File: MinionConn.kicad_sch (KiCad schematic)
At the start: 16 parts, among them J1 MinionConn, U2 EL817

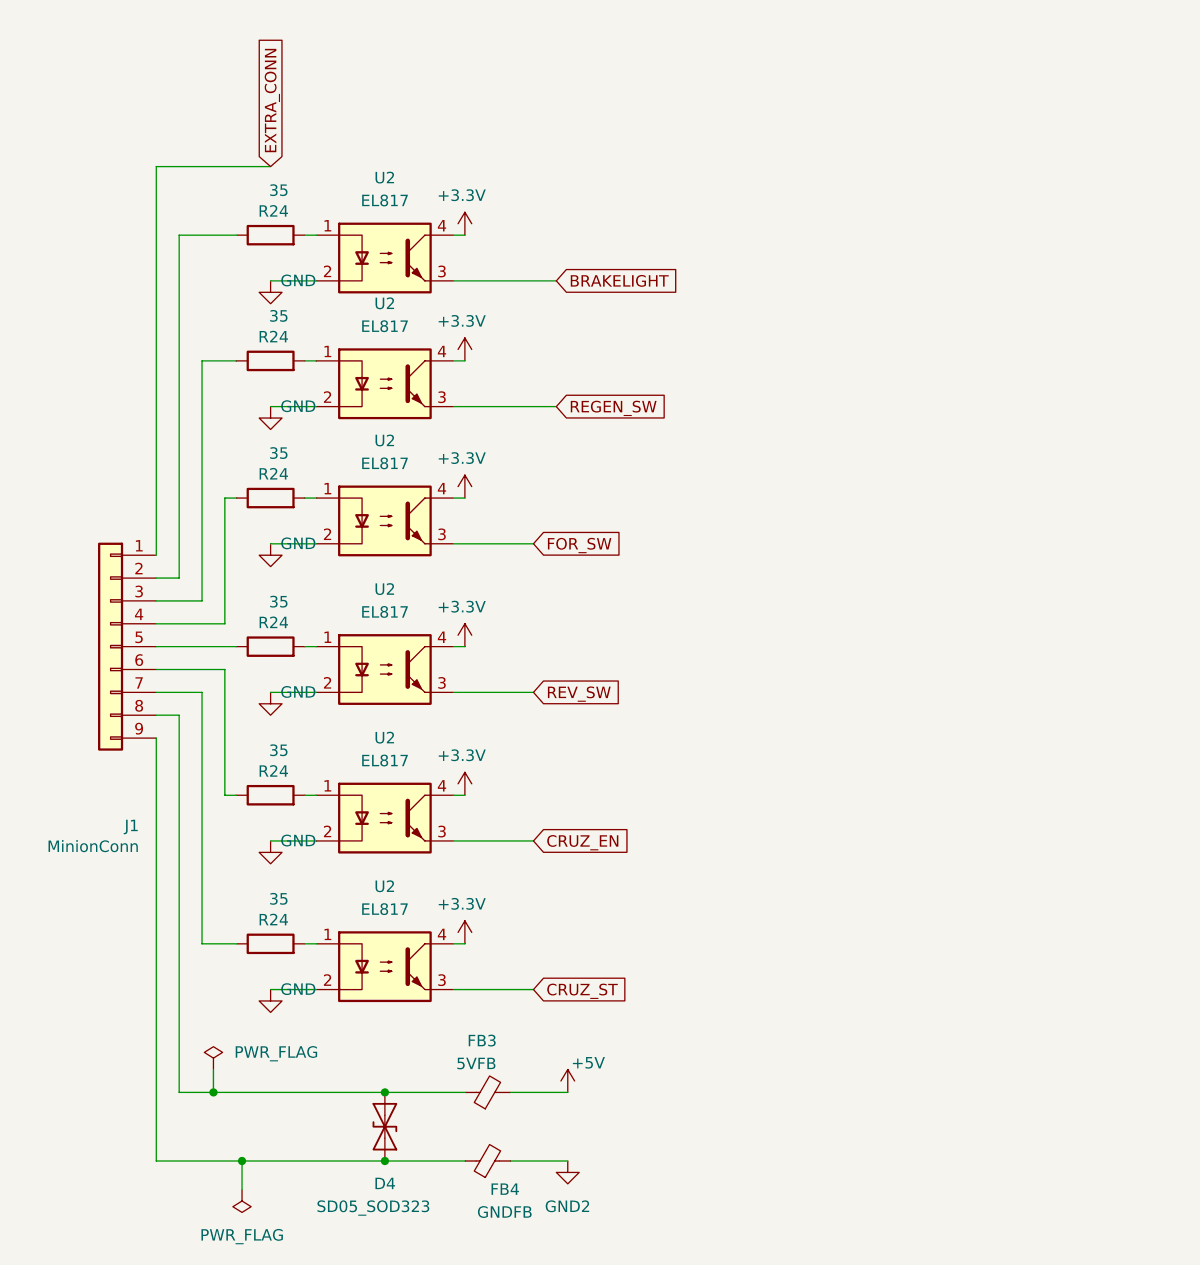
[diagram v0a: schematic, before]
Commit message: Opto-Isolators now interface mosfets to avoid ground problems, also separated 12V 'power' ground and ground passed from minion connector
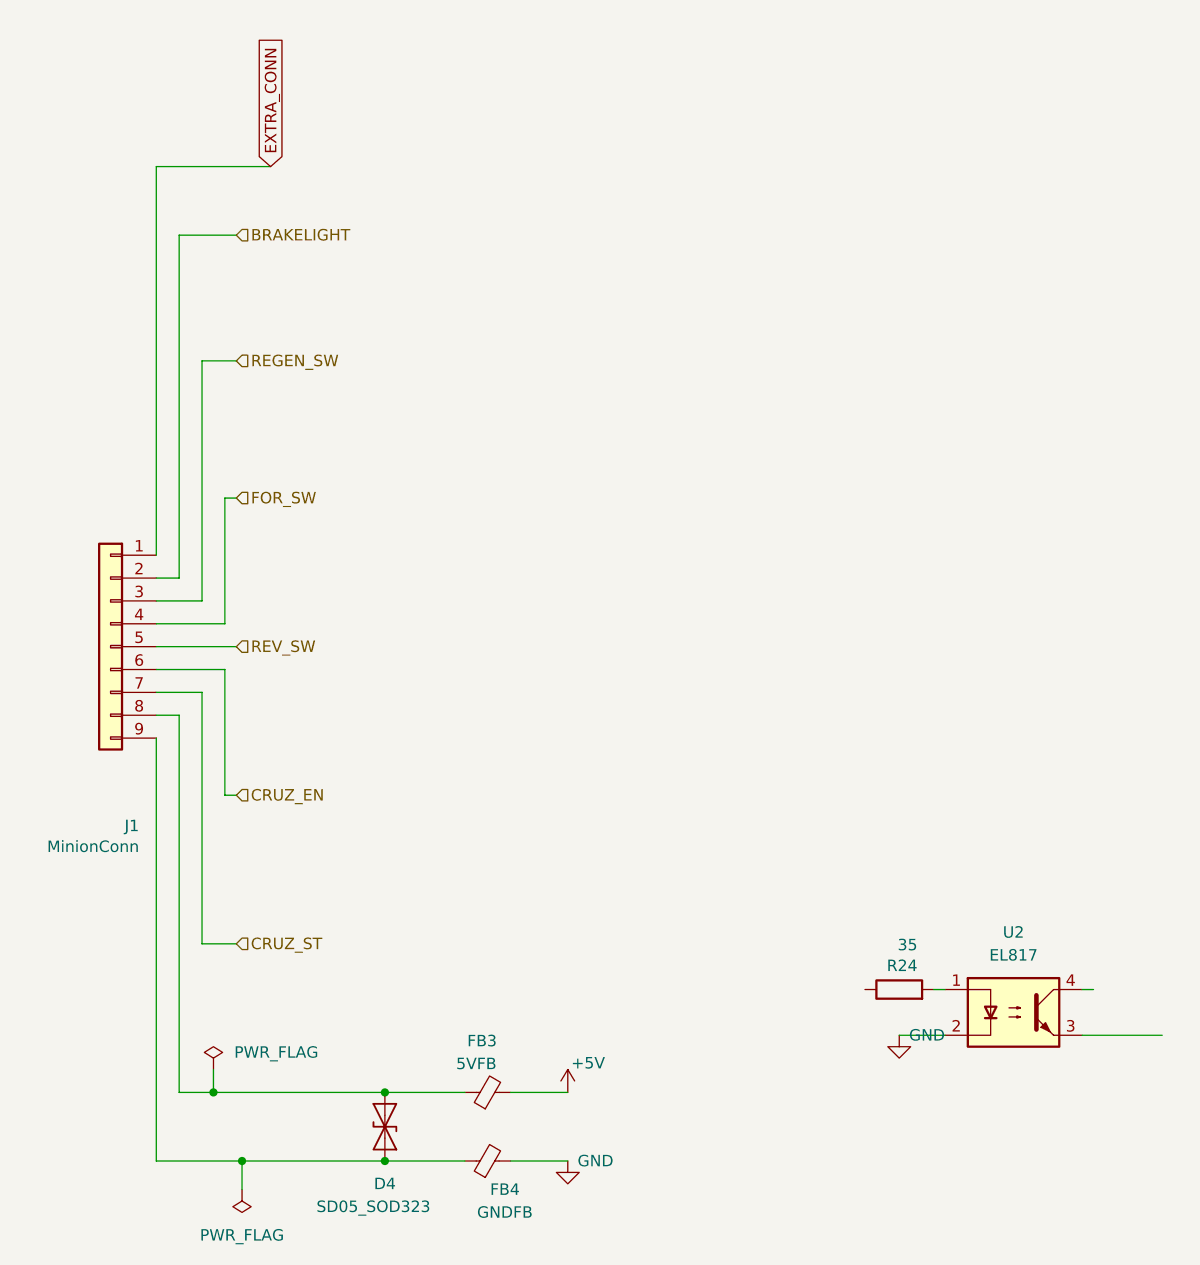
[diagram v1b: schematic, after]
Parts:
- removed R24 (x6): 35, Resistor_SMD:R_0805_2012Metric, symbol Device:R
- removed U2 (x6): EL817, Package_DIP:DIP-4_W7.62mm, symbol Isolator:EL817
- added R24: 35, Resistor_SMD:R_0805_2012Metric, symbol Device:R
- added U2: EL817, Package_DIP:DIP-4_W7.62mm, symbol Isolator:EL817
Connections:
- net GND2 is gone; now on net GND: FB4.2
- net BRAKELIGHT: now also J1.2 (Pin_2)
- net CRUZ_EN: now also J1.6 (Pin_6)
- net CRUZ_ST: now also J1.7 (Pin_7)
- net FOR_SW: now also J1.4 (Pin_4)
- net GND: now also U2.2
- net REGEN_SW: now also J1.3 (Pin_3)
- net REV_SW: now also J1.5 (Pin_5)
- new net: R24.2, U2.1

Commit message: Did layout
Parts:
- removed D4: SD05_SOD323, Diode_SMD:D_SOD-323, symbol Diode:SD05_SOD323
- removed R24: 35, Resistor_SMD:R_0805_2012Metric, symbol Device:R
- removed U2: EL817, Package_DIP:DIP-4_W7.62mm, symbol Isolator:EL817
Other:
- moved on the sheet: FB3, FB4

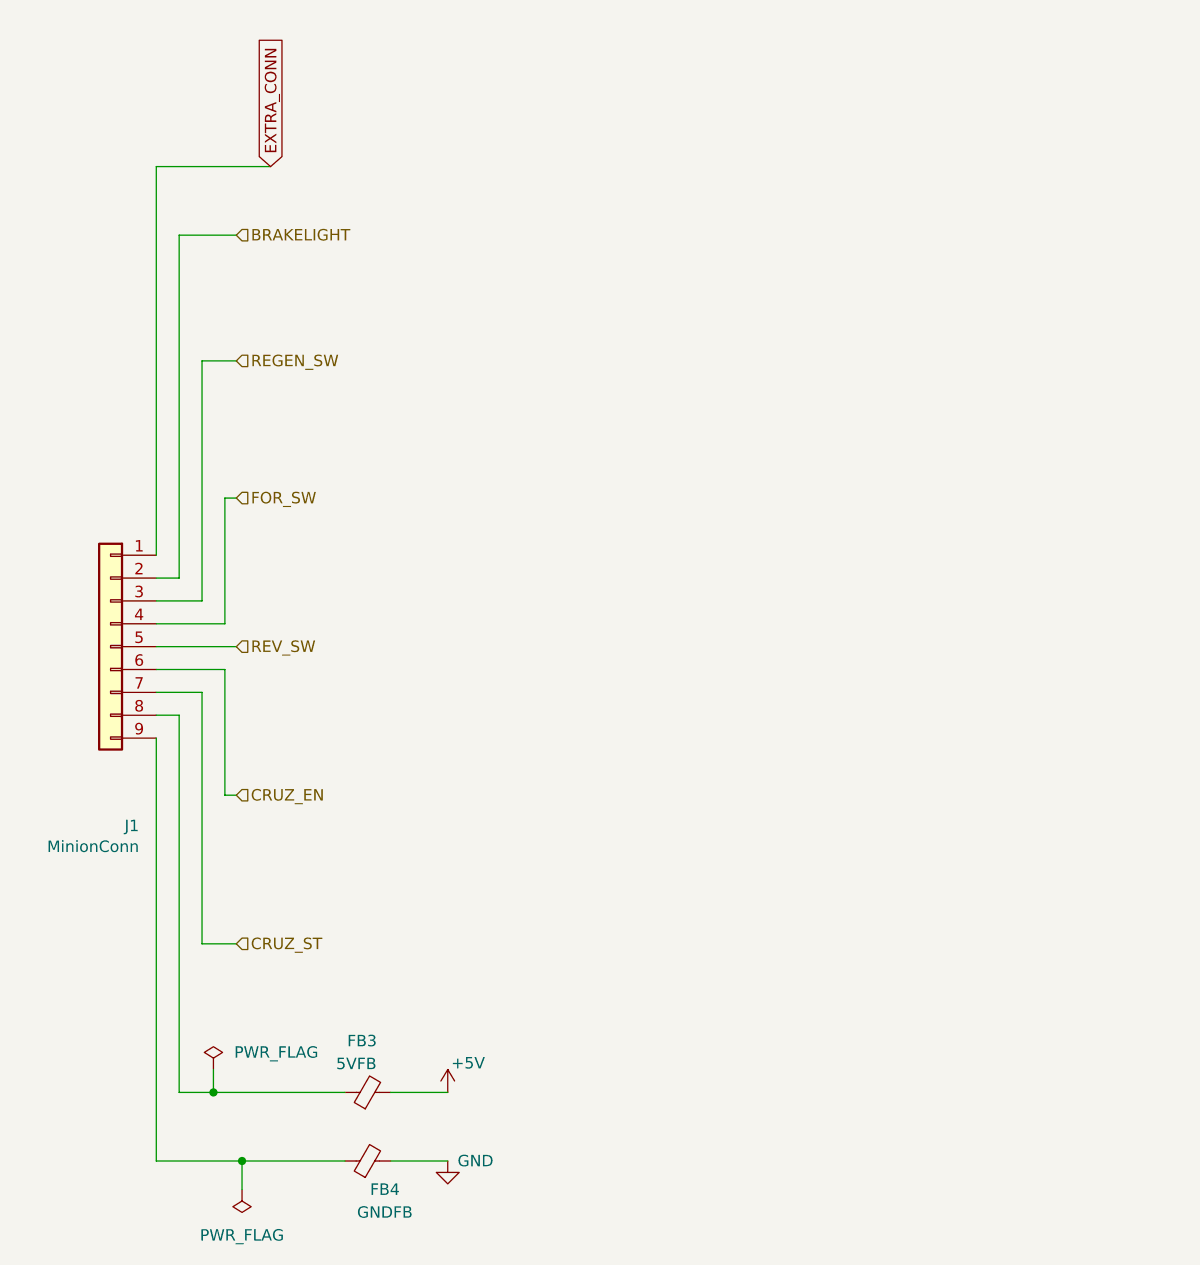
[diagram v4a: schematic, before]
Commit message: replaced gate driver and updated limiting resistor, added psom connector (made no connections yet)
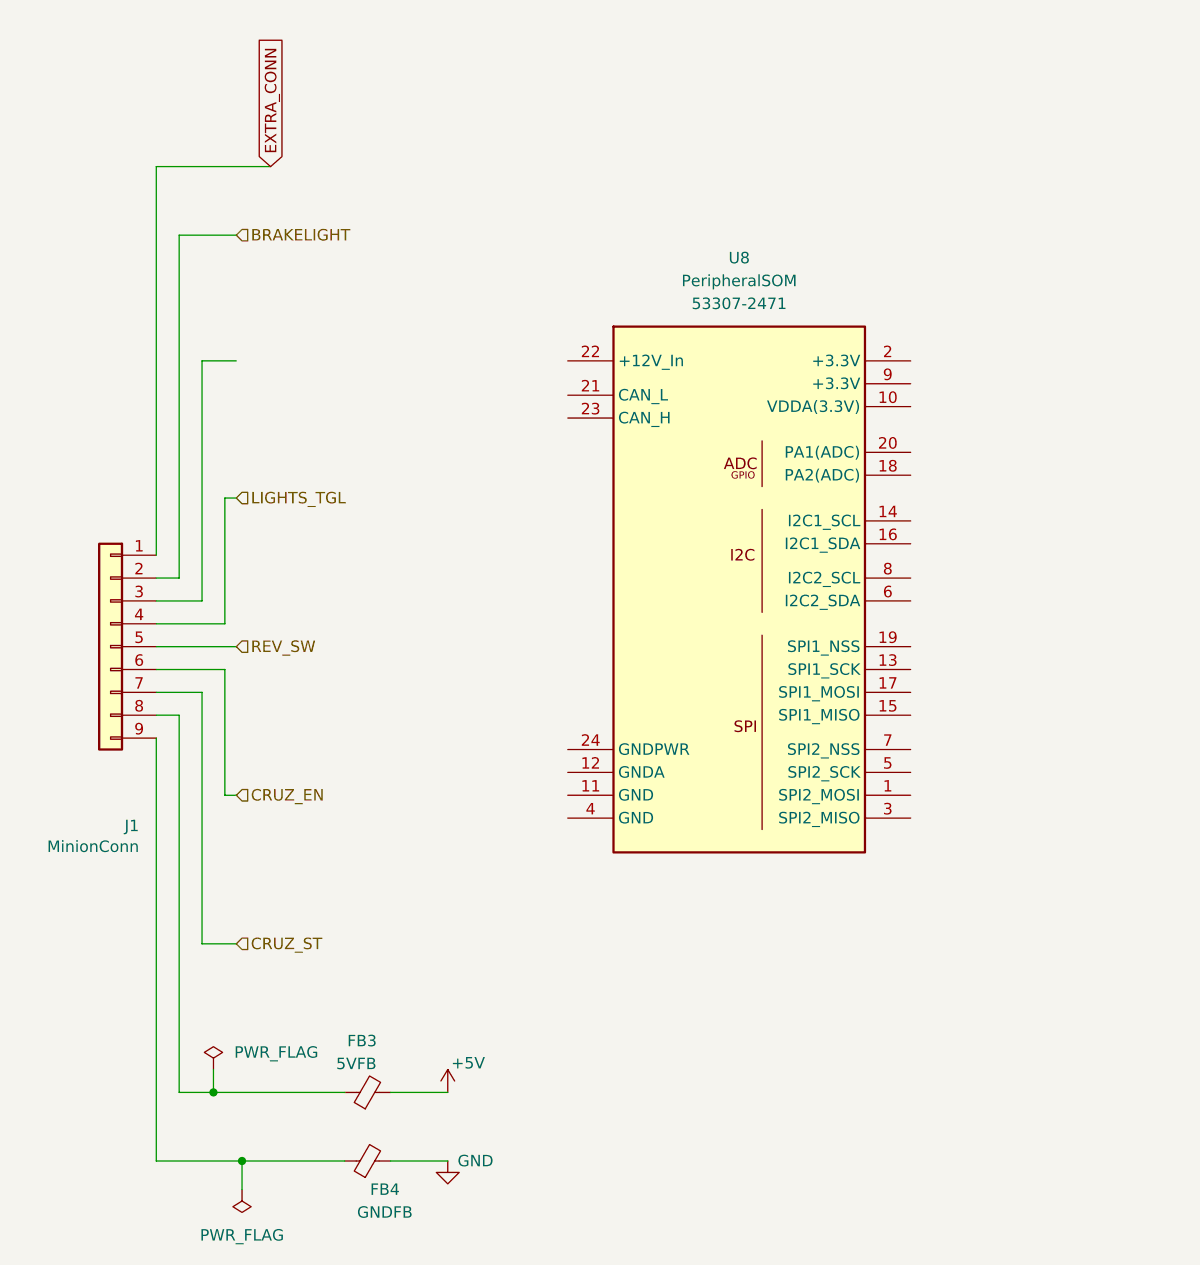
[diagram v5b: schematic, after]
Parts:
- added U8: PeripheralSOM, UTSVT_Special:PeripheralSOM, symbol utsvt-misc:PeripheralSOM
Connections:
- net FOR_SW renamed LIGHTS_TGL
- net REGEN_SW: no longer names the net of J1.3 (Pin_3)
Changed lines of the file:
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@@
 		)
 	)
-	(hierarchical_label "FOR_SW"
+	(hierarchical_label "LIGHTS_TGL"
 		(shape input)
 		(at 38.1 66.04 0)
@@
 		(shape input)
 		(at 38.1 99.06 0)
-		(fields_autoplaced yes)
-		(effects
-			(font
-				(size 1.27 1.27)
-			)
-			(justify left)
-		)
-	)
-	(hierarchical_label "REGEN_SW"
-		(shape input)
-		(at 38.1 50.8 0)
 		(fields_autoplaced yes)
 		(effects
@@
 					(unit 1)
 				)
+			)
+		)
+	)
+	(symbol
+		(lib_id "utsvt-misc:PeripheralSOM")
+		(at 93.98 76.2 0)
+		(unit 1)
+		(exclude_from_sim no)
+		(in_bom yes)
+		(on_board yes)
+		(dnp no)
+		(fields_autoplaced yes)
+		(property "Reference" "U8"
+			(at 93.98 39.37 0)
+			(effects
+				(font
+					(size 1.27 1.27)
+				)
+			)
+		)
+		(property "Value" "PeripheralSOM"
+			(at 93.98 41.91 0)
+			(effects
+				(font
+					(size 1.27 1.27)
+				)
+			)
+		)
+		(property "Footprint" "UTSVT_Special:PeripheralSOM"
+			(at 19.558 31.242 0)
+			(effects
+				(font
+					(size 1.27 1.27)
+				)
+				(hide yes)
+			)
+		)
+		(property "Datasheet" "https://tools.molex.com/pdm_docs/sd/533072071_sd.pdf"
+			(at 18.034 28.956 0)
+			(effects
+				(font
+					(size 1.27 1.27)
+				)
+				(hide yes)
+			)
+		)
+		(property "Description" ""
+			(at 96.52 52.07 0)
+			(effects
+				(font
+					(size 1.27 1.27)
+				)
+				(hide yes)
+			)
+		)
+		(property "P/N" "53307-2471"
+			(at 93.98 44.45 0)
+			(effects
+				(font
+					(size 1.27 1.27)
+				)
+			)
+		)
+		(property "Height" "3.85"
+			(at 93.98 76.2 0)
+			(effects
+				(font
+					(size 1.27 1.27)
+				)
+				(hide yes)
+			)
+		)
+		(pin "22"
+		)
+		(pin "8"
+		)
+		(pin "2"
+		)
+		(pin "14"
+		)
+		(pin "6"
+		)
+		(pin "4"
+		)
+		(pin "17"
+		)
+		(pin "24"
+		)
+		(pin "5"
+		)
+		(pin "18"
+		)
+		(pin "19"
+		)
+		(pin "16"
+		)
+		(pin "9"
+		)
+		(pin "1"
+		)
+		(pin "15"
+		)
+		(pin "23"
+		)
+		(pin "13"
+		)
+		(pin "7"
+		)
+		(pin "11"
+		)
+		(pin "3"
+		)
+		(pin "21"
+		)
+		(pin "12"
+		)
+		(pin "20"
+		)
+		(pin "10"
+		)
+		(instances
+			(project "Controls-LightingPCB"
+				(path "/229b82f0-5048-47d6-8bc8-0bcee42eb4bc/878def96-76f6-45ed-b005-573a6523d263"
+					(reference "U8")
+					(unit 1)
+				)

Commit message: schematic complete (?)
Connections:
- net BRAKELIGHT: now also U8.8 (I2C2_SCL)
- net LIGHTS_TGL: now also U8.6 (I2C2_SDA)
- net +3.3V: now reaches U8.2 (+3.3V)
- net +12V: now reaches U8.22 (+12V_In)
